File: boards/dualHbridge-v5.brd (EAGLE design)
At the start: 50.8 x 50.8 mm, 23 parts, among them Q1 IRLML0060, Q2 IRLML0060, Q3 IRLML0060, Q4 IRLML0060, Q5 IRLML0060, Q6 IRLML0060, Q7 IRLML0060, Q8 IRLML0060, X1 SPRING-TERMINAL, X2 SPRING-TERMINAL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

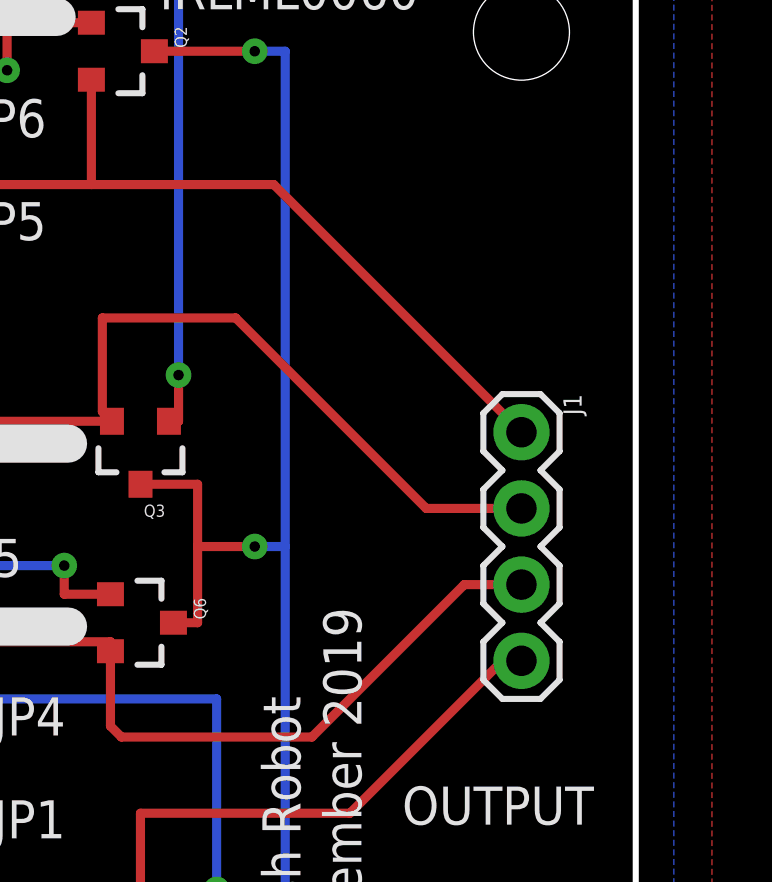
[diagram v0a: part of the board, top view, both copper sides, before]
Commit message: added readme  with linked bom
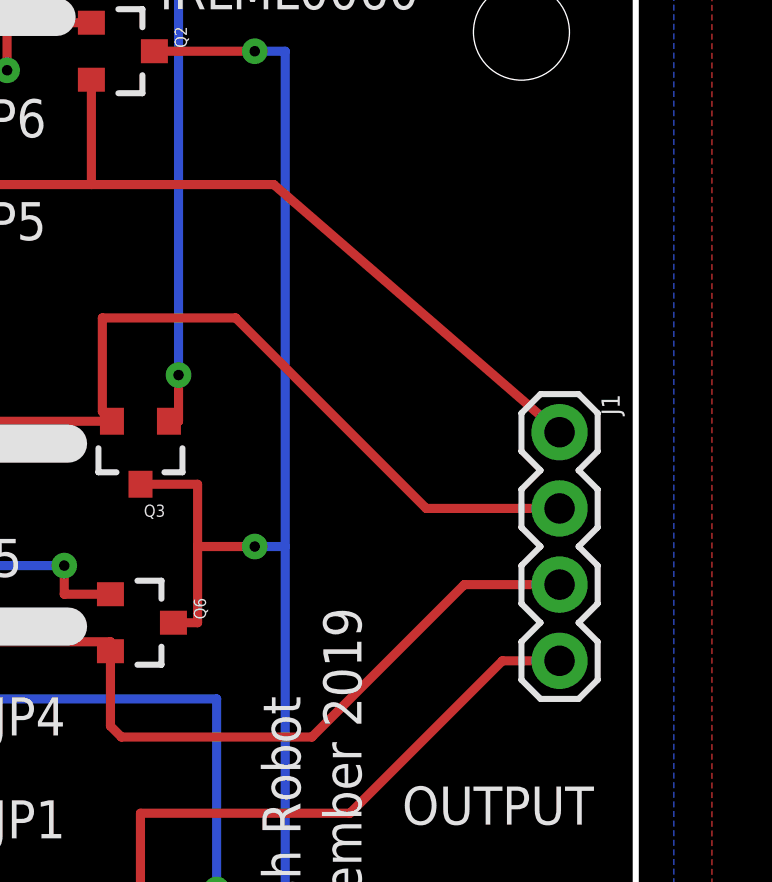
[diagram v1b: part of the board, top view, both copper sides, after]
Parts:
- moved J1 1.27 mm to (48.3, 33.7)
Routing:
- net B-: track 37.7 -> 38.9 mm
- net B+: track 42.2 -> 43.5 mm
- net A-: track 42.1 -> 43.4 mm
- net A+: track 37.7 -> 38.6 mm
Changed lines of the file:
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@@
 <element name="Q2" library="spietz-library" package="SOT-23" value="IRLML0060" x="33.655" y="46.355" rot="R270"/>
 <element name="Q1" library="spietz-library" package="SOT-23" value="IRLML0060" x="20.955" y="46.355" rot="R180"/>
-<element name="J1" library="SparkFun-Connectors" package="1X04" value="" x="46.99" y="33.655" rot="R270">
-<attribute name="PROD_ID" value="CONN-09696" x="46.99" y="33.655" size="1.778" layer="27" rot="R270" display="off"/>
+<element name="J1" library="SparkFun-Connectors" package="1X04" value="" x="48.26" y="33.655" rot="R270">
+<attribute name="PROD_ID" value="CONN-09696" x="48.26" y="33.655" size="1.778" layer="27" rot="R270" display="off"/>
 </element>
 <element name="R1" library="SparkFun-Resistors" package="0603" value="10k" x="12.065" y="10.16" rot="R90">
@@
 <wire x1="33.02" y1="37.465" x2="37.465" y2="37.465" width="0.3048" layer="1"/>
 <wire x1="37.465" y1="37.465" x2="43.815" y2="31.115" width="0.3048" layer="1"/>
-<wire x1="43.815" y1="31.115" x2="46.99" y2="31.115" width="0.3048" layer="1"/>
+<wire x1="43.815" y1="31.115" x2="48.26" y2="31.115" width="0.3048" layer="1"/>
 </signal>
 <signal name="A+">
@@
 <contactref element="Q1" pad="3"/>
 <contactref element="J1" pad="1"/>
-<wire x1="46.99" y1="33.655" x2="38.735" y2="41.91" width="0.3048" layer="1"/>
+<wire x1="48.26" y1="33.655" x2="38.735" y2="41.91" width="0.3048" layer="1"/>
 <wire x1="27.559" y1="41.91" x2="27.559" y2="41.656" width="0.3048" layer="1"/>
 <wire x1="38.735" y1="41.91" x2="32.655" y2="41.91" width="0.3048" layer="1"/>
@@
 <wire x1="34.29" y1="20.955" x2="41.275" y2="20.955" width="0.3048" layer="1"/>
 <wire x1="41.275" y1="20.955" x2="46.355" y2="26.035" width="0.3048" layer="1"/>
-<wire x1="46.355" y1="26.035" x2="46.99" y2="26.035" width="0.3048" layer="1"/>
+<wire x1="46.355" y1="26.035" x2="48.26" y2="26.035" width="0.3048" layer="1"/>
 </signal>
 <signal name="B+">
@@
 <wire x1="33.655" y1="23.495" x2="40.005" y2="23.495" width="0.3048" layer="1"/>
 <wire x1="40.005" y1="23.495" x2="45.085" y2="28.575" width="0.3048" layer="1"/>
-<wire x1="45.085" y1="28.575" x2="46.99" y2="28.575" width="0.3048" layer="1"/>
+<wire x1="45.085" y1="28.575" x2="48.26" y2="28.575" width="0.3048" layer="1"/>
 <wire x1="22.055" y1="26.67" x2="28.194" y2="26.67" width="0.3048" layer="1"/>
 <wire x1="28.194" y1="26.67" x2="33.29" y2="26.67" width="0.3048" layer="1"/>
